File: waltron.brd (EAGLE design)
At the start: 55.2 x 46.3 mm, 26 parts, among them IC1 4049N, IC2 LM386, J1 On Switch, J2 9v battery, J7 8ohm speaker

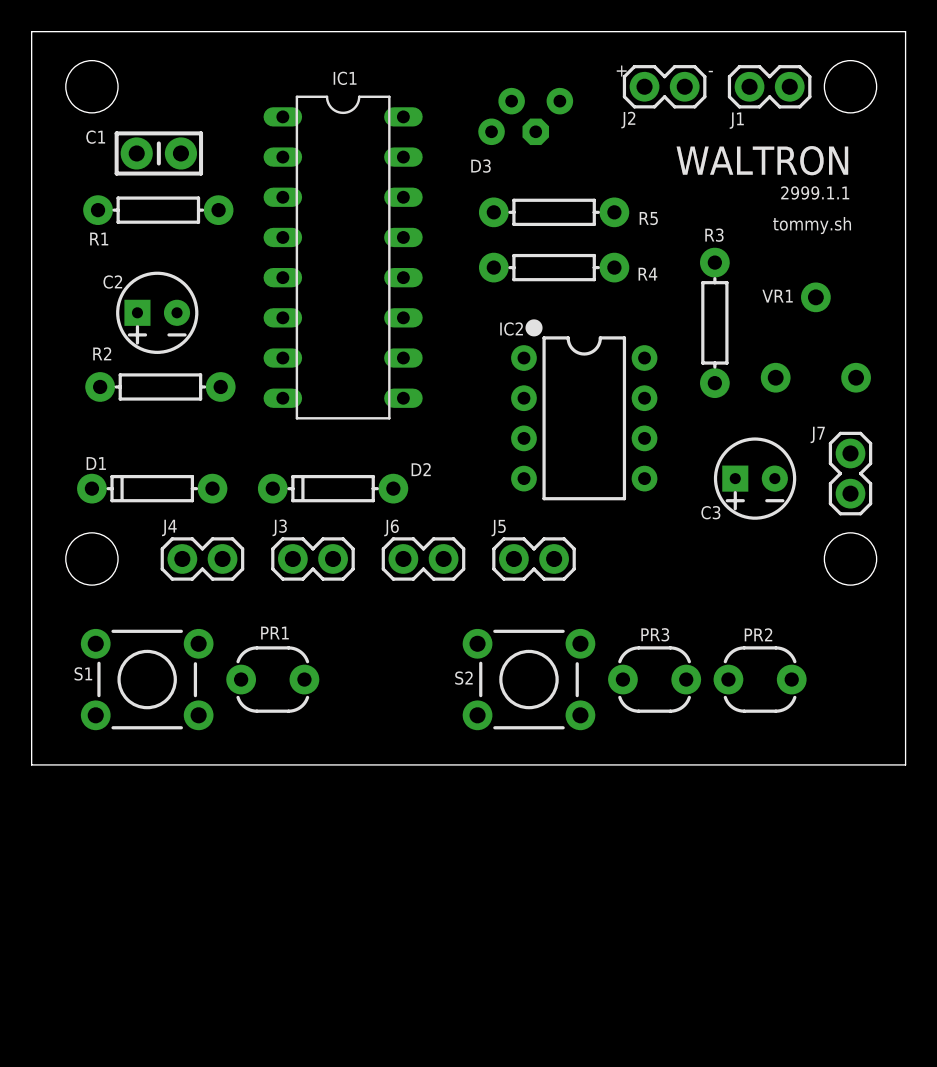
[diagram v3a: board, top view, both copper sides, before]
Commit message: Remove headers, re-layout buttons+sensore, layout all
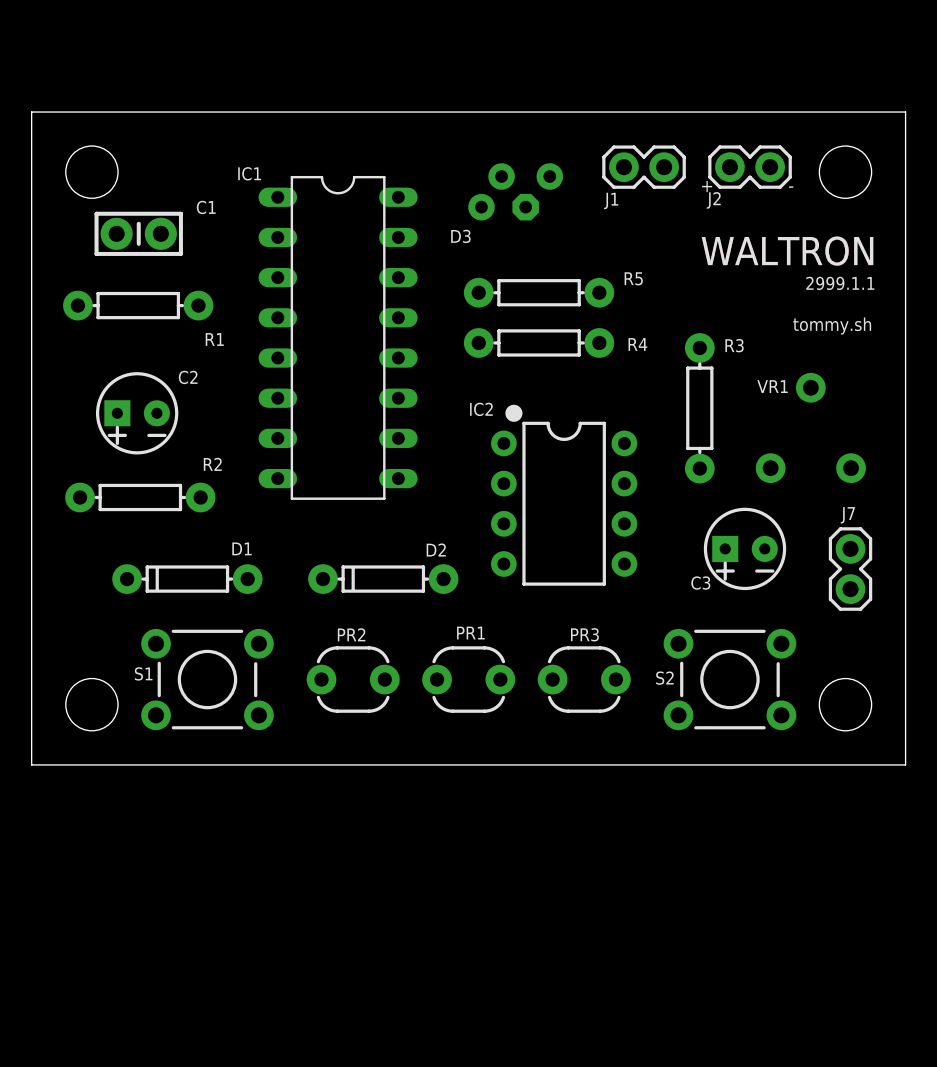
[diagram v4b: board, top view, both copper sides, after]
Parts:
- removed J3, J4, J5, J6: (no value), SparkFun-Connectors:1X02
- moved PR2 25.7 mm to (20.3, 5.40)
- moved S2 12.7 mm to (44.1, 5.40)
- moved PR1 12.4 mm to (27.6, 5.40)
- moved J1 9.42 mm to (37.4, 37.8)
- moved J2 7.41 mm to (44.1, 37.8)
- moved R2 7.10 mm to (6.87, 16.9)
- moved D2 6.54 mm to (22.2, 11.7)
- moved C2 6.48 mm to (6.67, 22.2)
- moved R1 6.16 mm to (6.74, 29.0)
- moved D1 6.13 mm to (9.84, 11.7)
- moved J7 6.03 mm to (51.8, 11.1)
- moved VR1 5.72 mm to (49.2, 18.8)
- moved IC2 5.54 mm to (33.7, 16.5)
- moved R3 5.48 mm to (42.2, 22.5)
- moved C1 5.24 mm to (6.77, 33.6)
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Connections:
- net N$11: no longer J6.1
- net N$12: no longer J4.2, J6.2
- net N$3: no longer J3.1
- net N$4: no longer J3.2
- net N$5: no longer J5.1
- net N$8: no longer J5.2
- net N$9: no longer J4.1
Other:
- board size 55.2 x 46.3 mm -> 55.2 x 41.3 mm

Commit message: Autoroute and finish 2999.1.1
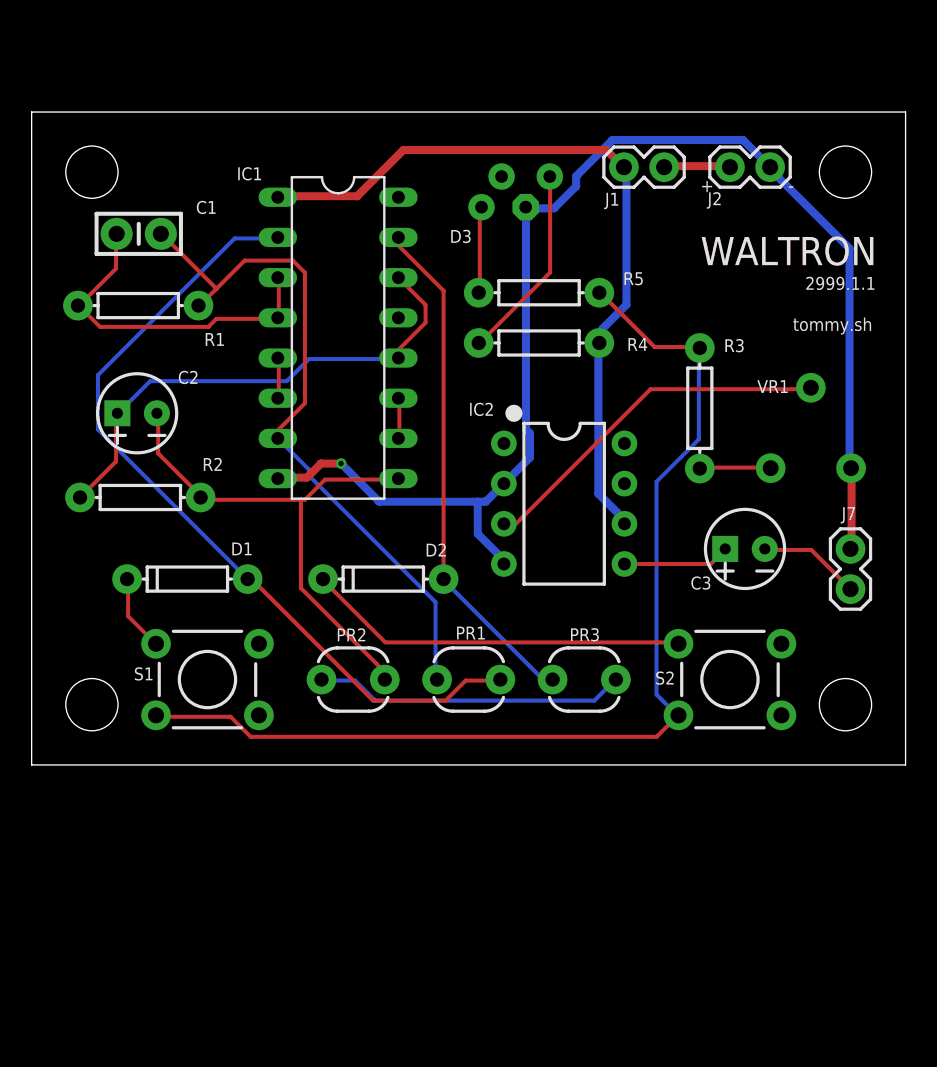
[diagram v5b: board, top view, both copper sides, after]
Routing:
- net GND: track 0.00 -> 83.7 mm, vias 0 -> 1
- net N$12: track 0.00 -> 66.9 mm
- net N$4: track 0.00 -> 51.5 mm
- net V+: track 0.00 -> 47.6 mm
- net N$3: track 0.00 -> 43.8 mm
- net N$5: track 0.00 -> 33.2 mm
- net N$8: track 0.00 -> 32.3 mm
- net N$7: track 0.00 -> 32.1 mm
- net N$11: track 0.00 -> 24.2 mm
- net N$16: track 0.00 -> 23.0 mm
- net N$2: track 0.00 -> 21.6 mm
- net N$10: track 0.00 -> 19.7 mm
- net N$18: track 0.00 -> 12.4 mm
- net N$14: track 0.00 -> 6.78 mm
- net N$15: track 0.00 -> 6.49 mm
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
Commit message: Put LED on top, re-route
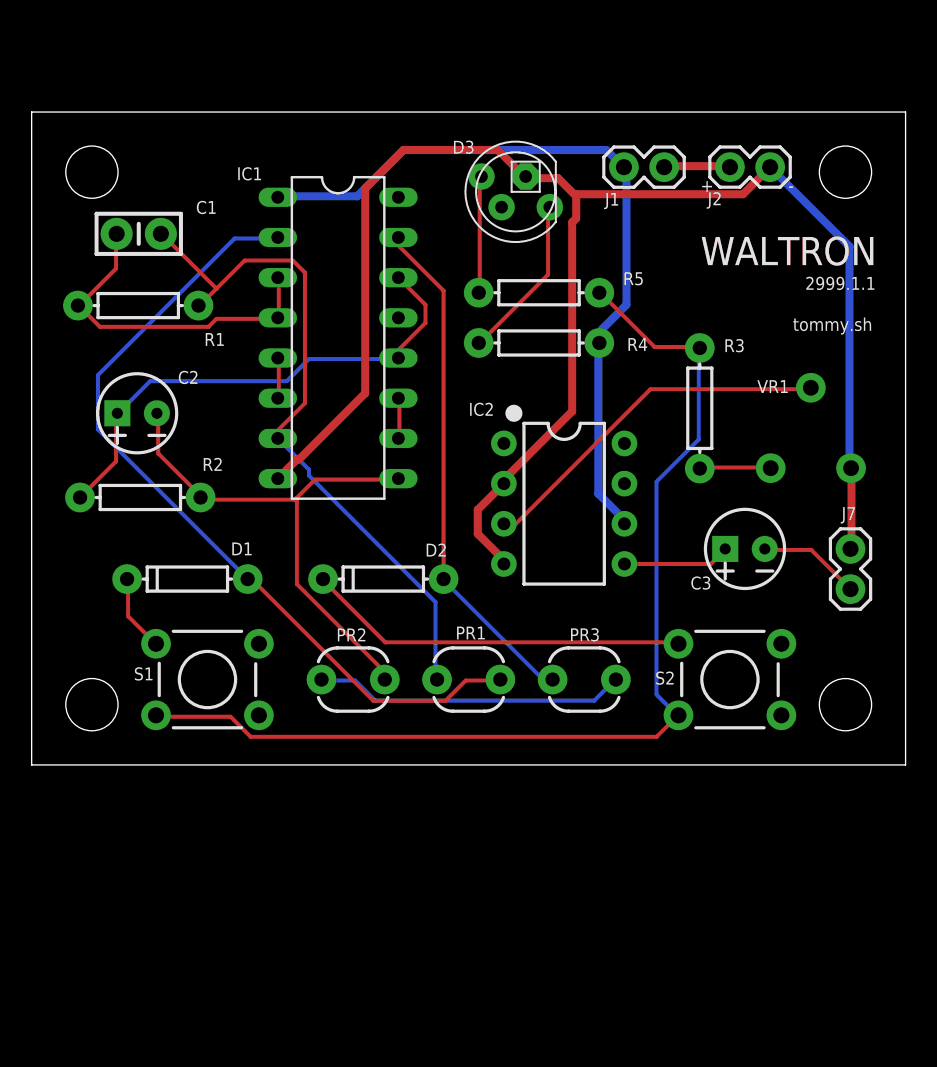
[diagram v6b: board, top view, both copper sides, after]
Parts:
- flipped D3 to the bottom, turned to 180 degrees
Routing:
- net GND: track 83.7 -> 102.1 mm, vias 1 -> 0
- net N$18: track 12.4 -> 10.5 mm
- net N$17: track 5.53 -> 7.45 mm

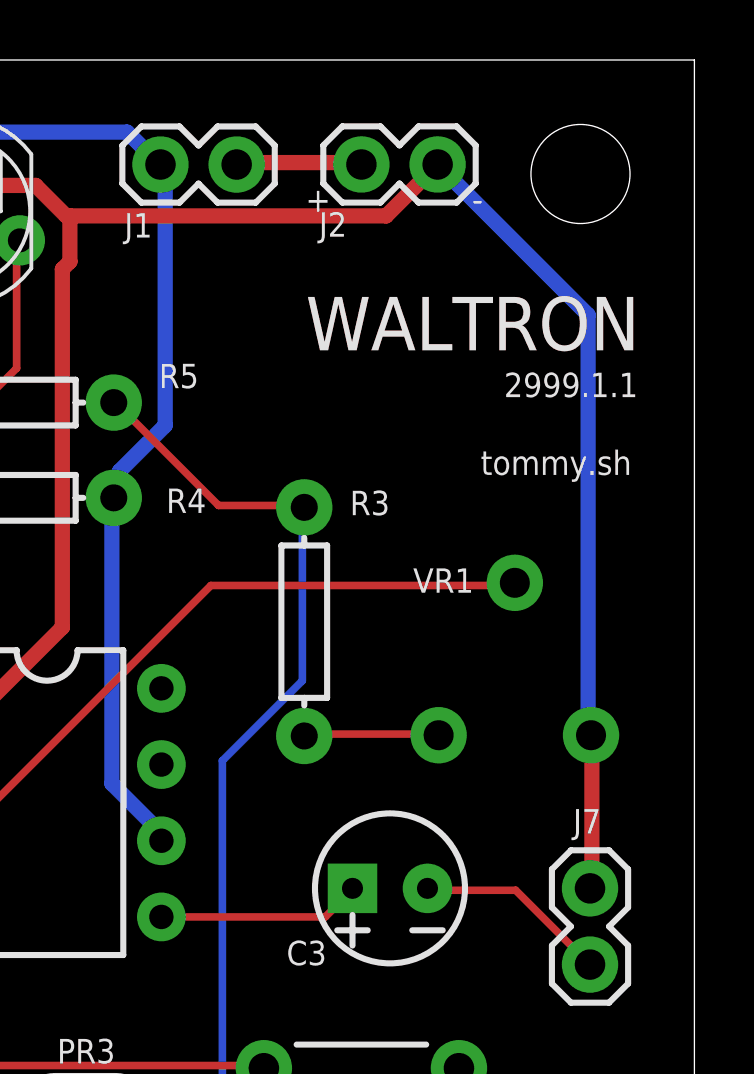
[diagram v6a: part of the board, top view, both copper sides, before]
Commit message: Reverse volume knob rotation
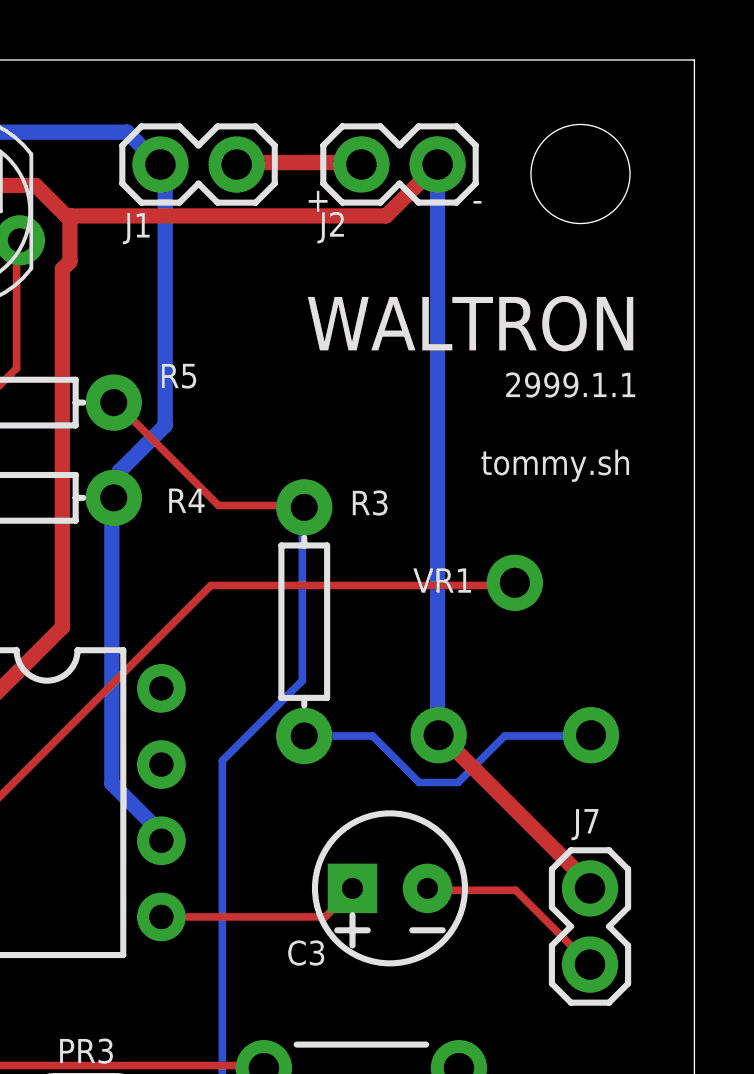
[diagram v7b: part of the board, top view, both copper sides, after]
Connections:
- net GND: now also VR1.2; no longer VR1.3
- net N$13: now also VR1.3; no longer VR1.2
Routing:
- net N$13: track 4.51 -> 10.9 mm
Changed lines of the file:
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@@
 <?xml version="1.0" encoding="utf-8"?>
 <!DOCTYPE eagle SYSTEM "eagle.dtd">
-<eagle version="8.1.0">
+<eagle version="8.2.2">
 <drawing>
 <settings>
@@
 <contactref element="J2" pad="2"/>
 <contactref element="IC1" pad="8"/>
-<contactref element="VR1" pad="3"/>
 <contactref element="D3" pad="3"/>
-<wire x1="51.816" y1="18.669" x2="51.816" y2="13.716" width="0.508" layer="1"/>
 <wire x1="51.816" y1="13.716" x2="51.7525" y2="13.6525" width="0.508" layer="1"/>
-<wire x1="51.816" y1="18.669" x2="51.786546875" y2="18.75783125" width="0.508" layer="1"/>
 <wire x1="29.845" y1="12.954" x2="29.845" y2="12.7" width="0.508" layer="1"/>
 <wire x1="28.194" y1="14.605" x2="29.845" y2="12.954" width="0.508" layer="1"/>
@@
 <wire x1="31.115" y1="37.211" x2="29.464" y2="38.862" width="0.508" layer="1"/>
 <wire x1="31.115" y1="37.211" x2="31.224234375" y2="37.189690625" width="0.508" layer="1"/>
-<wire x1="44.958" y1="36.068" x2="46.6725" y2="37.7825" width="0.508" layer="1"/>
+<wire x1="46.6725" y1="37.7825" x2="44.958" y2="36.068" width="0.508" layer="1"/>
 <wire x1="34.29" y1="36.068" x2="34.417" y2="36.068" width="0.508" layer="1"/>
 <wire x1="34.417" y1="36.068" x2="44.958" y2="36.068" width="0.508" layer="1"/>
@@
 <wire x1="34.417" y1="36.068" x2="34.417" y2="34.544" width="0.508" layer="1"/>
 <wire x1="29.972" y1="17.907" x2="29.845" y2="17.78" width="0.508" layer="1"/>
-<wire x1="51.689" y1="32.766" x2="51.689" y2="18.796" width="0.508" layer="16"/>
-<wire x1="46.6725" y1="37.7825" x2="51.689" y2="32.766" width="0.508" layer="16"/>
-<wire x1="51.689" y1="18.796" x2="51.786546875" y2="18.75783125" width="0.508" layer="16"/>
-</signal>
-<signal name="N$13">
-<contactref element="R3" pad="P$2"/>
 <contactref element="VR1" pad="2"/>
-<wire x1="46.609" y1="18.796" x2="42.291" y2="18.796" width="0.254" layer="1"/>
-<wire x1="42.291" y1="18.796" x2="42.2275" y2="18.7325" width="0.254" layer="1"/>
-<wire x1="46.609" y1="18.796" x2="46.706546875" y2="18.75783125" width="0.254" layer="1"/>
+<wire x1="46.706546875" y1="18.75783125" x2="46.77416875" y2="18.75783125" width="0.508" layer="1"/>
+<wire x1="46.77416875" y1="18.75783125" x2="51.816" y2="13.716" width="0.508" layer="1"/>
+<wire x1="46.6725" y1="37.7825" x2="46.6725" y2="18.791878125" width="0.508" layer="16"/>
+<wire x1="46.6725" y1="18.791878125" x2="46.706546875" y2="18.75783125" width="0.508" layer="16"/>
 </signal>
 <signal name="N$16">
@@
 <wire x1="44.069" y1="37.846" x2="44.1325" y2="37.7825" width="0.508" layer="1"/>
 </signal>
+<signal name="N$13">
+<contactref element="R3" pad="P$2"/>
+<contactref element="VR1" pad="3"/>
+<wire x1="46.054240625" y1="17.183028125" x2="47.358853125" y2="17.183028125" width="0.254" layer="16"/>
+<wire x1="42.2275" y1="18.7325" x2="44.50476875" y2="18.7325" width="0.254" layer="16"/>
+<wire x1="44.50476875" y1="18.7325" x2="46.054240625" y2="17.183028125" width="0.254" layer="16"/>
+<wire x1="47.358853125" y1="17.183028125" x2="48.908325" y2="18.7325" width="0.254" layer="16"/>
+<wire x1="51.761215625" y1="18.7325" x2="51.786546875" y2="18.75783125" width="0.254" layer="16"/>
+<wire x1="48.908325" y1="18.7325" x2="51.761215625" y2="18.7325" width="0.254" layer="16"/>
+</signal>
 </signals>
